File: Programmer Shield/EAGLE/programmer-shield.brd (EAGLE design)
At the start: 63.5 x 39.4 mm, 7 parts

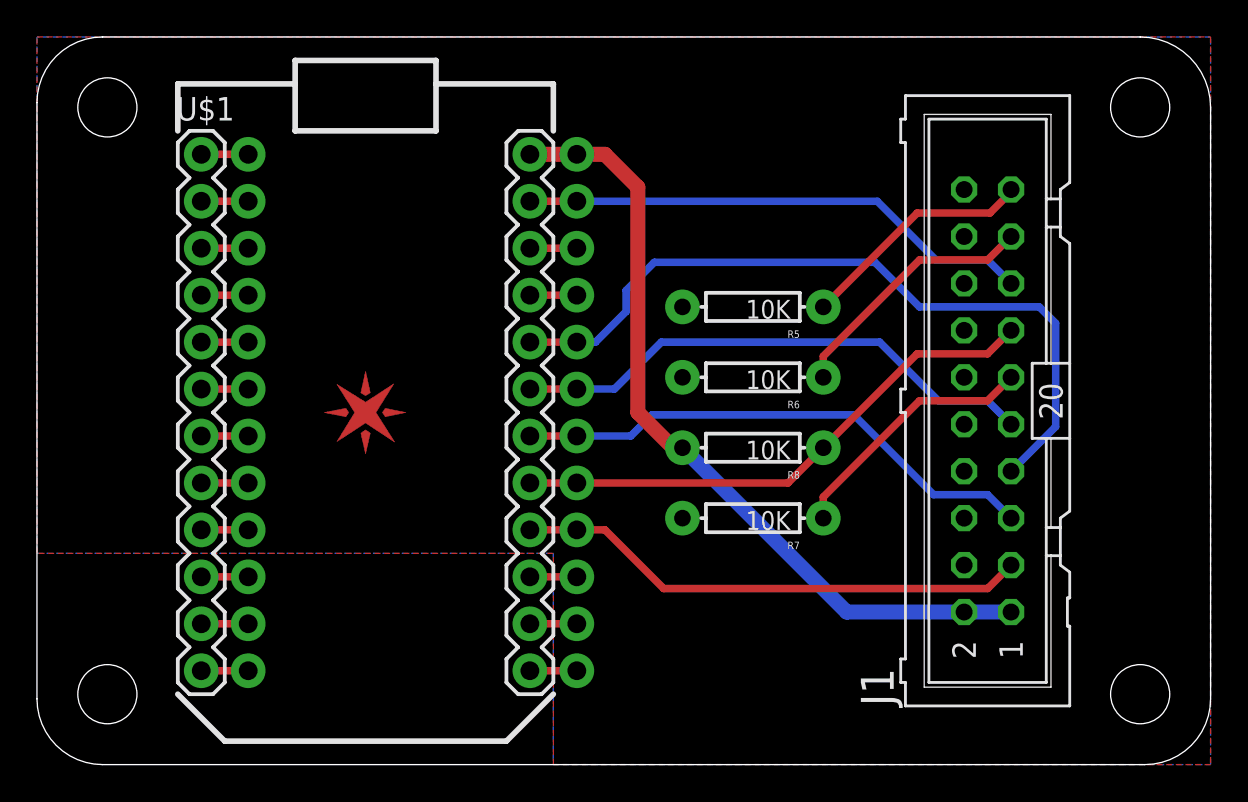
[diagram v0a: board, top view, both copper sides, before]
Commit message: updated shield BOMs and boards
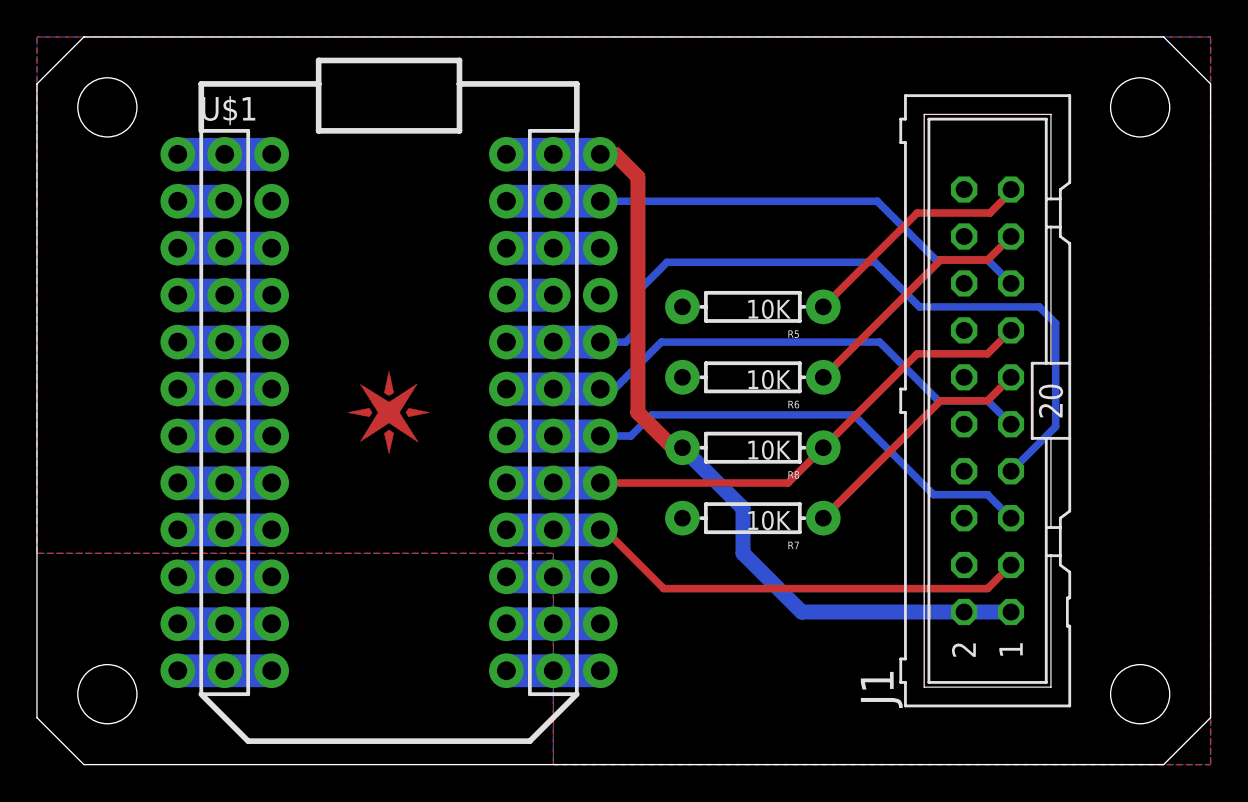
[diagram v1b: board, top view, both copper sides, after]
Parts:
- added LOGO1: OSHW-LOGOM, Spark:OSHW-LOGO-M
- moved E$1 1.27 mm to (19.1, 19.1)
- moved U$1 1.27 mm to (19.1, 19.1)
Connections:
- net !RST: now also U$1.#23
- net +3V3: now also U$1.#24
- net GND: now also U$1.#2, U$1.#21
- net N$1: now also U$1.#1
- net N$10: now also U$1.#11
- net N$11: now also U$1.#12
- net N$12: now also U$1.#13
- net N$16: now also U$1.#14
- net N$17: now also U$1.#15
- net N$18: now also U$1.#22
- net N$2: now also U$1.#3
- net N$3: now also U$1.#4
- net N$4: now also U$1.#5
- net N$5: now also U$1.#6
- net N$6: now also U$1.#7
- net N$7: now also U$1.#8
- net N$8: now also U$1.#9
- net N$9: now also U$1.#10
- net TCK: now also U$1.#19
- net TDI: now also U$1.#18
- net TDO: now also U$1.#17
- net TMS: now also U$1.#20
- net TRST: now also U$1.#16
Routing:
- net TMS: track 41.3 -> 45.2 mm
- net +3V3: track 43.4 -> 46.5 mm
- net N$18: track 2.54 -> 5.08 mm
- net N$17: track 2.54 -> 5.08 mm
- net N$16: track 2.54 -> 5.08 mm
- net N$12: track 2.54 -> 5.08 mm
- net N$9: track 2.54 -> 5.08 mm
- net N$8: track 2.54 -> 5.08 mm
- net N$7: track 2.54 -> 5.08 mm
- net N$6: track 2.54 -> 5.08 mm
- net N$5: track 2.54 -> 5.08 mm
- net N$4: track 2.54 -> 5.08 mm
- net N$3: track 2.54 -> 5.08 mm
- net N$2: track 2.54 -> 5.08 mm
- net N$11: track 2.54 -> 5.08 mm
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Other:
- outline, holes or cut-outs redrawn
- board text added: "Programmer Shield v2.0 sparkdevices.com"
- board text removed: "Spark Devices JTAG Shield"

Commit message: added license info to all design files
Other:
- board text added: "Reference Designs ARE PROVIDED "AS IS" AND "WITH ALL FAULTS. SPARK LABS, INC ("SPARK") DISCLAIMS ALL OTHER WARRANTIES, EXPRESS OR IMPLIED, REGARDING PRODUCTS OR THE REFERENCE DESIGNS, INCLUDING BUT NOT LIMITED TO, ANY IMPLIED WARRANTIES OF MERCHANTABILITY, FITNESS FOR A PARTICULAR PURPOSE, OR NON-INFRINGEMENT. Spark may make changes to specifications and product descriptions at any time, without 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"
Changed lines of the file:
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@@
 <dimension x1="3.81" y1="3.81" x2="3.81" y2="35.56" x3="-2.54" y3="19.685" layer="51"/>
 <dimension x1="3.81" y1="35.56" x2="59.69" y2="35.56" x3="31.75" y3="41.91" layer="51"/>
+<text x="109.22" y="5.08" size="1.4224" layer="51">Reference Designs ARE PROVIDED "AS IS" AND "WITH ALL FAULTS. SPARK LABS, INC
+("SPARK") DISCLAIMS ALL OTHER WARRANTIES, EXPRESS OR IMPLIED, REGARDING
+PRODUCTS OR THE REFERENCE DESIGNS, INCLUDING BUT NOT LIMITED TO, ANY
+IMPLIED WARRANTIES OF MERCHANTABILITY, FITNESS FOR A PARTICULAR PURPOSE,
+OR NON-INFRINGEMENT.
+Spark may make changes to specifications and product descriptions at any
+time, without notice. The Customer must not rely on the absence or
+characteristics of any features or instructions marked "reserved" or
+"undefined." Spark reserves these for future definition and shall have
+no responsibility whatsoever for conflicts or incompatibilities arising
+from future changes to them. The product information on the Web Site or
+Materials is subject to change without notice. Do not finalize a design
+with this information.
+Spark is a registered trademark.</text>
+<wire x1="104.14" y1="0" x2="104.14" y2="38.1" width="0.4064" layer="51"/>
+<wire x1="104.14" y1="38.1" x2="208.28" y2="38.1" width="0.4064" layer="51"/>
+<wire x1="208.28" y1="38.1" x2="208.28" y2="0" width="0.4064" layer="51"/>
+<wire x1="208.28" y1="0" x2="104.14" y2="0" width="0.4064" layer="51"/>
 </plain>
 <attributes>

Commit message: updated sshield and pshield gerbers
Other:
- board text added: "Programmer Shield v2.0.1 spark.io"
- board text removed: "Programmer Shield v2.0 sparkdevices.com"
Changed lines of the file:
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@@
 <?xml version="1.0" encoding="utf-8"?>
 <!DOCTYPE eagle SYSTEM "eagle.dtd">
-<eagle version="6.3">
+<eagle version="6.5.0">
 <drawing>
 <settings>
@@
 <board>
 <plain>
-<text x="56.388" y="33.782" size="1.778" layer="22" font="vector" ratio="10" rot="MR0">Programmer Shield v2.0
-sparkdevices.com</text>
+<text x="56.388" y="33.782" size="1.778" layer="22" font="vector" ratio="10" rot="MR0">Programmer Shield v2.0.1
+spark.io</text>
 <hole x="59.69" y="35.56" drill="3.2"/>
 <hole x="59.69" y="3.81" drill="3.2"/>
 <hole x="3.81" y="3.81" drill="3.2"/>
 <hole x="3.81" y="35.56" drill="3.2"/>
-<dimension x1="0" y1="-2.54" x2="63.5" y2="-2.54" x3="31.75" y3="-6.35" layer="51"/>
-<dimension x1="63.5" y1="0" x2="63.5" y2="39.37" x3="69.85" y3="19.685" layer="51"/>
+<dimension x1="0" y1="-2.54" x2="63.5" y2="-2.54" x3="31.75" y3="-6.35" textsize="3.5" layer="51"/>
+<dimension x1="63.5" y1="0" x2="63.5" y2="39.37" x3="69.85" y3="19.685" textsize="3.5" layer="51"/>
 <wire x1="2.54" y1="0" x2="0" y2="2.54" width="0" layer="20"/>
 <wire x1="0" y1="36.83" x2="2.54" y2="39.37" width="0" layer="20"/>
@@
 <wire x1="2.54" y1="39.37" x2="60.96" y2="39.37" width="0" layer="20"/>
 <wire x1="0" y1="2.54" x2="0" y2="36.83" width="0" layer="20"/>
-<dimension x1="3.81" y1="3.81" x2="3.81" y2="35.56" x3="-2.54" y3="19.685" layer="51"/>
-<dimension x1="3.81" y1="35.56" x2="59.69" y2="35.56" x3="31.75" y3="41.91" layer="51"/>
+<dimension x1="3.81" y1="3.81" x2="3.81" y2="35.56" x3="-2.54" y3="19.685" textsize="3.5" layer="51"/>
+<dimension x1="3.81" y1="35.56" x2="59.69" y2="35.56" x3="31.75" y3="41.91" textsize="3.5" layer="51"/>
 <text x="109.22" y="5.08" size="1.4224" layer="51">Reference Designs ARE PROVIDED "AS IS" AND "WITH ALL FAULTS. SPARK LABS, INC
 ("SPARK") DISCLAIMS ALL OTHER WARRANTIES, EXPRESS OR IMPLIED, REGARDING
